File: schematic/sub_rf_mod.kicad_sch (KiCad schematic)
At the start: 36 parts, among them J4B1 Conn_01x08

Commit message: first draft of board with components added, no traces
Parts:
- RF_JP1: footprint Resistor_THT:R_Axial_DIN0204_L3.6mm_D1.6mm_P7.62mm_Horizontal -> Resistor_THT:R_Axial_DIN0207_L6.3mm_D2.5mm_P15.24mm_Horizontal
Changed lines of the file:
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@@
       (effects (font (size 1.27 1.27)) (justify right))
     )
-    (property "Footprint" "Resistor_THT:R_Axial_DIN0204_L3.6mm_D1.6mm_P7.62mm_Horizontal" (id 2) (at 153.67 59.69 0)
+    (property "Footprint" "Resistor_THT:R_Axial_DIN0207_L6.3mm_D2.5mm_P15.24mm_Horizontal" (id 2) (at 153.67 59.69 0)
       (effects (font (size 1.27 1.27)) hide)
     )

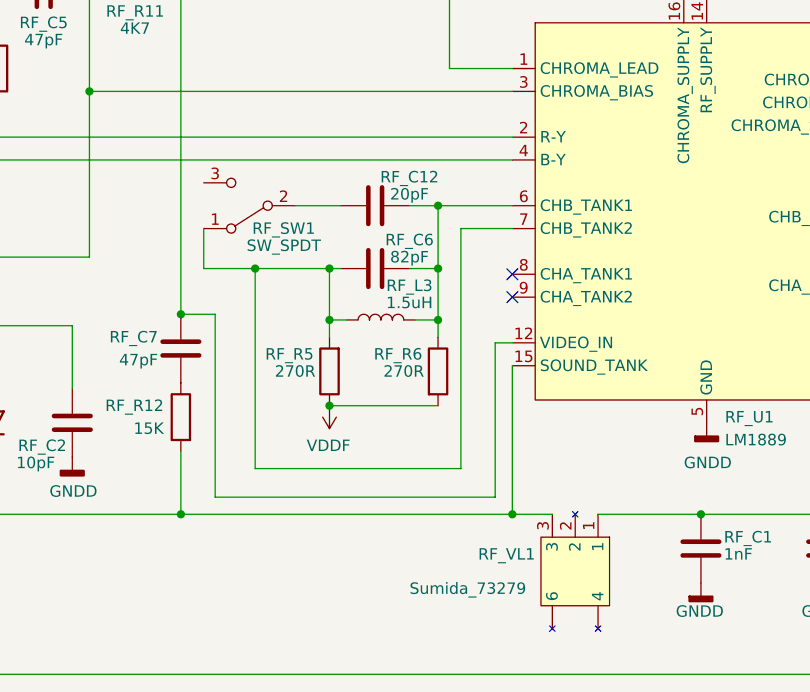
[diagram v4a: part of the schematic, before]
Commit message: did a small amount of pcb work, also finished component directions for the main board. RF pcb is still a mess and needs a second pass.
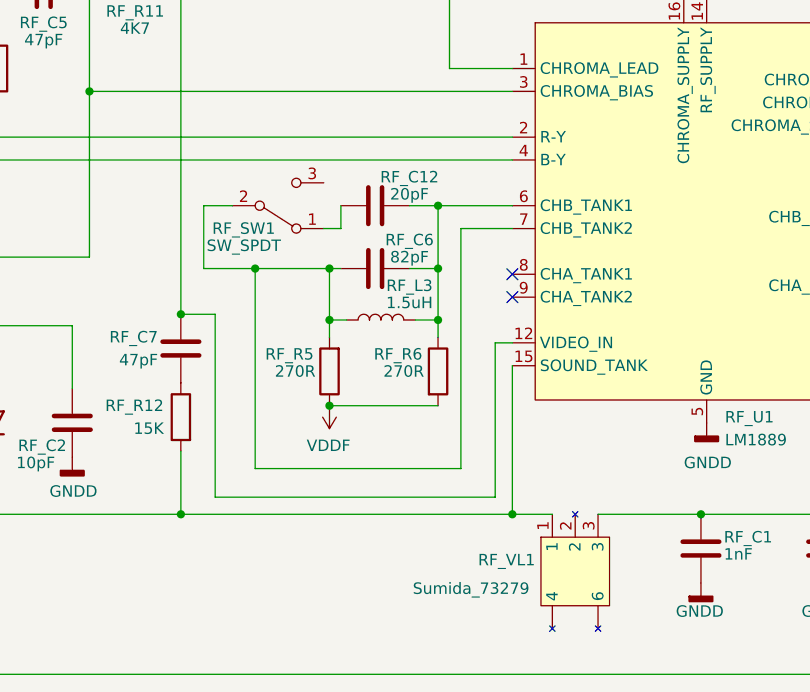
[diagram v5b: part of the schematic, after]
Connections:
- net at RF_C12.1: now also RF_SW1.1 (A); no longer RF_SW1.2 (B)
- net at RF_C1.1, RF_C8.1, RF_JP1.1 (A)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: now also RF_VL1.3; no longer RF_VL1.1
- net at RF_C6.1, RF_L3.1, RF_R5.2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: now also RF_SW1.2 (B); no longer RF_SW1.1 (A)
- net at RF_D2.1 (K), RF_R12.2, RF_U1.15 (SOUND_TANK): now also RF_VL1.1; no longer RF_VL1.3
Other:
- moved on the sheet: RF_SW1, RF_VL1
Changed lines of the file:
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@@
+    (stroke (width 0) (type default) (color 0 0 0 0))
+  )
+  (wire (pts (xy 100.33 99.06) (xy 100.33 92.075))
     (stroke (width 0) (type default) (color 0 0 0 0))
   )
@@
     (stroke (width 0) (type default) (color 0 0 0 0))
   )
+  (wire (pts (xy 115.57 92.075) (xy 115.57 94.615))
+    (stroke (width 0) (type default) (color 0 0 0 0))
+  )
   (wire (pts (xy 155.575 126.365) (xy 169.545 126.365))
     (stroke (width 0) (type default) (color 0 0 0 0))
@@
     (stroke (width 0) (type default) (color 0 0 0 0))
   )
-  (wire (pts (xy 100.33 99.06) (xy 100.33 94.615))
-    (stroke (width 0) (type default) (color 0 0 0 0))
-  )
   (wire (pts (xy 34.925 90.17) (xy 43.18 90.17))
     (stroke (width 0) (type default) (color 0 0 0 0))
@@
     (stroke (width 0) (type default) (color 0 0 0 0))
   )
+  (wire (pts (xy 115.57 94.615) (xy 113.665 94.615))
+    (stroke (width 0) (type default) (color 0 0 0 0))
+  )
   (wire (pts (xy 77.47 67.945) (xy 77.47 73.025))
     (stroke (width 0) (type default) (color 0 0 0 0))
@@
     (stroke (width 0) (type default) (color 0 0 0 0))
   )
-  (wire (pts (xy 110.49 92.075) (xy 115.57 92.075))
-    (stroke (width 0) (type default) (color 0 0 0 0))
-  )
   (wire (pts (xy 34.925 95.25) (xy 43.18 95.25))
+    (stroke (width 0) (type default) (color 0 0 0 0))
+  )
+  (wire (pts (xy 100.33 92.075) (xy 103.505 92.075))
     (stroke (width 0) (type default) (color 0 0 0 0))
   )
@@
     (pin "2")
   )
-  (symbol (lib_id "Switch:SW_SPDT") (at 105.41 92.075 180) (unit 1)
-    (in_bom yes) (on_board yes)
-    (property "Reference" "RF_SW1" (id 0) (at 109.22 94.615 0))
-    (property "Value" "SW_SPDT" (id 1) (at 109.22 96.52 0))
-    (property "Footprint" "Button_Switch_THT:SW_CuK_OS102011MA1QN1_SPDT_Angled" (id 2) (at 105.41 92.075 0)
-      (effects (font (size 1.27 1.27)) hide)
-    )
-    (property "Datasheet" "~" (id 3) (at 105.41 92.075 0)
+  (symbol (lib_id "Switch:SW_SPDT") (at 108.585 92.075 0) (mirror x) (unit 1)
+    (in_bom yes) (on_board yes)
+    (property "Reference" "RF_SW1" (id 0) (at 104.775 94.615 0))
+    (property "Value" "SW_SPDT" (id 1) (at 104.775 96.52 0))
+    (property "Footprint" "Button_Switch_THT:SW_CuK_OS102011MA1QN1_SPDT_Angled" (id 2) (at 108.585 92.075 0)
+      (effects (font (size 1.27 1.27)) hide)
+    )
+    (property "Datasheet" "~" (id 3) (at 108.585 92.075 0)
       (effects (font (size 1.27 1.27)) hide)
     )
@@
     (pin "2")
   )
-  (symbol (lib_id "Variable_Inductors:Sumida_73279") (at 141.605 132.715 270) (unit 1)
-    (in_bom yes) (on_board yes)
-    (property "Reference" "RF_VL1" (id 0) (at 130.81 130.81 90)
-      (effects (font (size 1.27 1.27)) (justify left))
-    )
-    (property "Value" "Sumida_73279" (id 1) (at 123.19 134.62 90)
-      (effects (font (size 1.27 1.27)) (justify left))
-    )
-    (property "Footprint" "Variable_Inductors:Sumida_73279" (id 2) (at 146.685 132.715 0)
-      (effects (font (size 1.27 1.27)) hide)
-    )
-    (property "Datasheet" "" (id 3) (at 146.685 132.715 0)
-      (effects (font (size 1.27 1.27)) hide)
-    )
+  (symbol (lib_id "Variable_Inductors:Sumida_73279") (at 141.605 132.715 90) (mirror x) (unit 1)
+    (in_bom yes) (on_board yes)
+    (property "Reference" "RF_VL1" (id 0) (at 137.16 131.445 90)
+      (effects (font (size 1.27 1.27)) (justify left))
+    )
+    (property "Value" "Sumida_73279" (id 1) (at 136.525 134.62 90)
+      (effects (font (size 1.27 1.27)) (justify left))
+    )
+    (property "Footprint" "Variable_Inductors:Sumida_73279" (id 2) (at 136.525 132.715 0)
+      (effects (font (size 1.27 1.27)) hide)
+    )
+    (property "Datasheet" "" (id 3) (at 136.525 132.715 0)
+      (effects (font (size 1.27 1.27)) hide)
+    )
